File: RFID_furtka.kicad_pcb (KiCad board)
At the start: 2 copper layers, 20 parts, among them J1 CONN_01X03, Q1 SI2300DS, SW1 TSC_RELAY, U1 LDF33DT-TR, U2 MFRC522, U3 nodemcu-devkit-v1.0(ESP8266)

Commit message: Add BOM
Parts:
- moved C9 36.7 mm to (147.4, 83.5), turned to 270 degrees
- moved C7 21.9 mm to (162.8, 93.6)
- moved C8 16.8 mm to (147.4, 103.8), turned to 90 degrees
- moved J1 4.13 mm to (133.0, 80.9), turned to 0 degrees
- moved C4 2.30 mm to (132.3, 117.4)
- moved U3 0.41 mm to (154.9, 99.9), turned to 180 degrees
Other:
- board outline added: 39.3 x 59.9 mm
- net class Default: clearance 0.2 -> 0.2032; trace_width 0.25 -> 0.254
- rule trace_clearance: 0.2 -> 0.2032
- rule trace_min: 0.2 -> 0.2032
- rule via_min_drill: 0.3 -> 0.4
- rule via_min_size: 0.4 -> 0.6

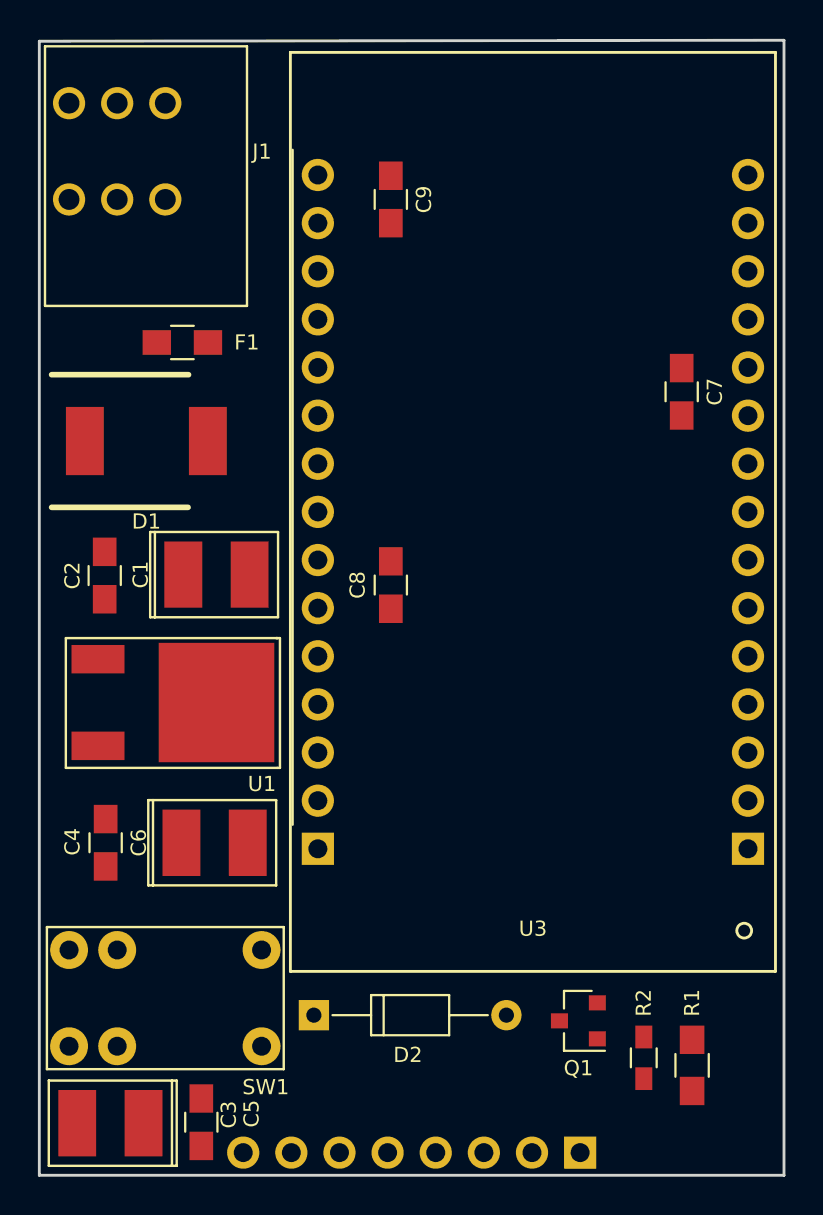
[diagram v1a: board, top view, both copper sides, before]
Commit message: Fix few 3D bugs
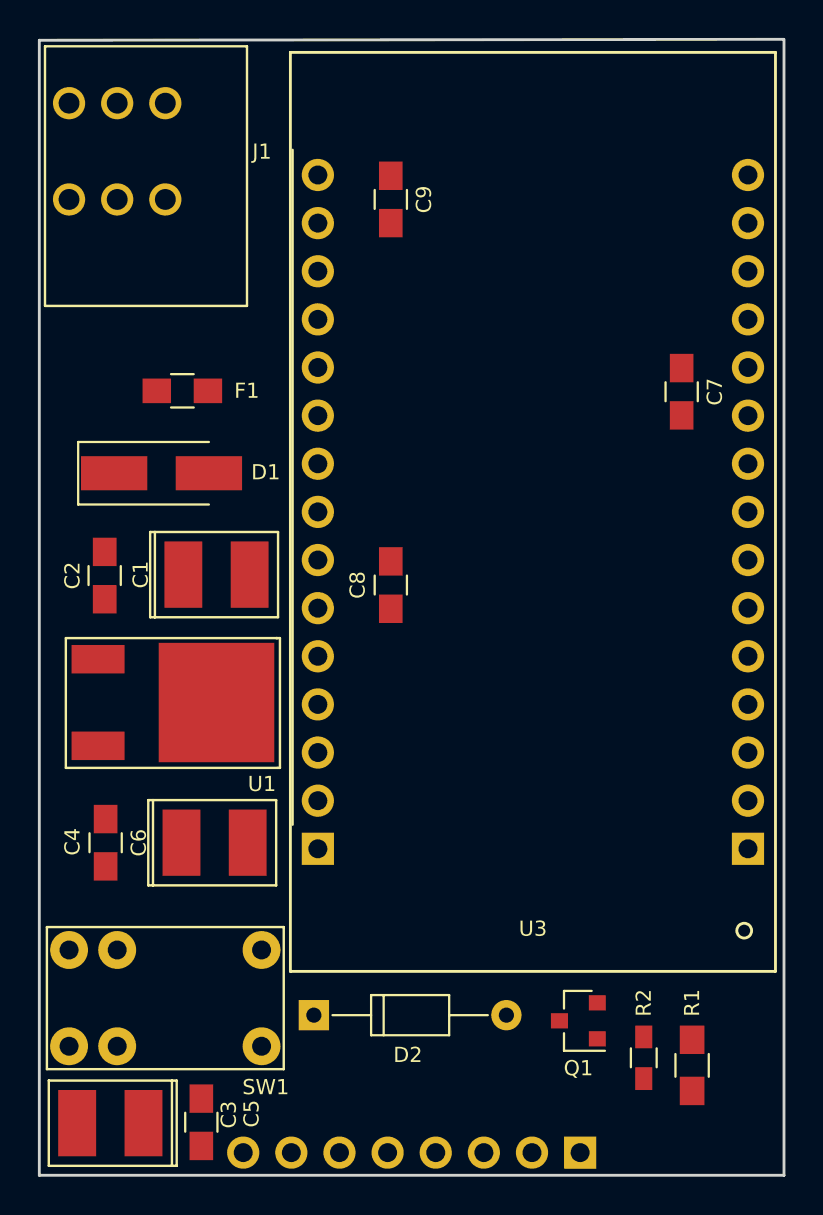
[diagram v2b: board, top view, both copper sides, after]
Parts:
- D1: footprint MyDiodesSMD:DO-214AB -> Diodes_SMD:D_SMA_Handsoldering
- moved F1 2.55 mm to (136.4, 93.5)
- moved D1 1.88 mm to (135.3, 97.9), turned to 0 degrees
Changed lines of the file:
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@@
     (links 51)
     (no_connects 51)
-    (area 127.0499 74.912899 168.341801 136.567486)
+    (area 128.774999 74.924999 168.225001 135.025001)
     (thickness 1.6)
     (drawings 4)
@@
     )
   )
-  (module MyDiodesSMD:DO-214AB (layer F.Cu)
-    (at 134.5 96.2 180)
-    (fp_text reference D1 (at 0 -4.25 180) (layer F.SilkS)
-      (effects (font (size 0.8 0.8) (thickness 0.15)))
-    )
-    (fp_text value SS34 (at -0.05 4.375 180) (layer F.Fab)
-      (effects (font (size 0.5 0.5) (thickness 0.125)))
-    )
-    (fp_line (start -5.275 3.8) (end -5.275 -3.75) (layer F.CrtYd) (width 0.1))
-    (fp_line (start 5.25 3.8) (end -5.275 3.8) (layer F.CrtYd) (width 0.1))
-    (fp_line (start 5.25 -3.775) (end 5.25 3.8) (layer F.CrtYd) (width 0.1))
-    (fp_line (start -5.25 -3.775) (end 5.25 -3.775) (layer F.CrtYd) (width 0.1))
-    (fp_line (start -2.225 3.5) (end 5 3.5) (layer F.SilkS) (width 0.3))
-    (fp_line (start -2.2 -3.5) (end 5 -3.5) (layer F.SilkS) (width 0.3))
-    (pad 1 smd rect (at 3.245 0 180) (size 2 3.6) (layers F.Cu F.Paste F.Mask)
-      (net 1 +12V))
-    (pad 2 smd rect (at -3.245 0 180) (size 2 3.6) (layers F.Cu F.Paste F.Mask)
-      (net 4 "Net-(D1-Pad2)"))
-    (model "My.3dshapes/DO-214AB(SMC).wrl"
-      (at (xyz 0 0 0))
-      (scale (xyz 0.3937 0.3937 0.3937))
-      (rotate (xyz 0 0 180))
-    )
-  )
   (module Diodes_THT:D_DO-35_SOD27_P10.16mm_Horizontal (layer F.Cu)
     (at 143.34 126.5)
@@
   )
   (module Resistors_SMD:R_0805_HandSoldering (layer F.Cu)
-    (at 136.4 91 180)
+    (at 136.4 93.55 180)
     (descr "Resistor SMD 0805, hand soldering")
     (tags "resistor 0805")
@@
       (at (xyz 0 0 0))
       (scale (xyz 1 1 1))
-      (rotate (xyz 0 0 0))
+      (rotate (xyz 0 0 90))
     )
   )
@@
     )
   )
-  (gr_line (start 168.15 75.05) (end 128.85 75.1) (layer Edge.Cuts) (width 0.15))
+  (module Diodes_SMD:D_SMA_Handsoldering (layer F.Cu)
+    (at 135.3 97.9)
+    (descr "Diode SMA (DO-214AC) Handsoldering")
+    (tags "Diode SMA (DO-214AC) Handsoldering")
+    (attr smd)
+    (fp_text reference D1 (at 5.5 -0.05) (layer F.SilkS)
+      (effects (font (size 0.8 0.8) (thickness 0.15)))
+    )
+    (fp_text value SS34 (at 0 2.6) (layer F.Fab)
+      (effects (font (size 1 1) (thickness 0.15)))
+    )
+    (fp_text user %R (at 0 -2.5) (layer F.Fab)
+      (effects (font (size 1 1) (thickness 0.15)))
+    )
+    (fp_line (start -4.4 -1.65) (end -4.4 1.65) (layer F.SilkS) (width 0.12))
+    (fp_line (start 2.3 1.5) (end -2.3 1.5) (layer F.Fab) (width 0.1))
+    (fp_line (start -2.3 1.5) (end -2.3 -1.5) (layer F.Fab) (width 0.1))
+    (fp_line (start 2.3 -1.5) (end 2.3 1.5) (layer F.Fab) (width 0.1))
+    (fp_line (start 2.3 -1.5) (end -2.3 -1.5) (layer F.Fab) (width 0.1))
+    (fp_line (start -4.5 -1.75) (end 4.5 -1.75) (layer F.CrtYd) (width 0.05))
+    (fp_line (start 4.5 -1.75) (end 4.5 1.75) (layer F.CrtYd) (width 0.05))
+    (fp_line (start 4.5 1.75) (end -4.5 1.75) (layer F.CrtYd) (width 0.05))
+    (fp_line (start -4.5 1.75) (end -4.5 -1.75) (layer F.CrtYd) (width 0.05))
+    (fp_line (start -0.64944 0.00102) (end -1.55114 0.00102) (layer F.Fab) (width 0.1))
+    (fp_line (start 0.50118 0.00102) (end 1.4994 0.00102) (layer F.Fab) (width 0.1))
+    (fp_line (start -0.64944 -0.79908) (end -0.64944 0.80112) (layer F.Fab) (width 0.1))
+    (fp_line (start 0.50118 0.75032) (end 0.50118 -0.79908) (layer F.Fab) (width 0.1))
+    (fp_line (start -0.64944 0.00102) (end 0.50118 0.75032) (layer F.Fab) (width 0.1))
+    (fp_line (start -0.64944 0.00102) (end 0.50118 -0.79908) (layer F.Fab) (width 0.1))
+    (fp_line (start -4.4 1.65) (end 2.5 1.65) (layer F.SilkS) (width 0.12))
+    (fp_line (start -4.4 -1.65) (end 2.5 -1.65) (layer F.SilkS) (width 0.12))
+    (pad 1 smd rect (at -2.5 0) (size 3.5 1.8) (layers F.Cu F.Paste F.Mask)
+      (net 1 +12V))
+    (pad 2 smd rect (at 2.5 0) (size 3.5 1.8) (layers F.Cu F.Paste F.Mask)
+      (net 4 "Net-(D1-Pad2)"))
+    (model Diodes_SMD.3dshapes/D_SMA_Handsoldering.wrl
+      (at (xyz 0 0 0))
+      (scale (xyz 0.3937 0.3937 0.3937))
+      (rotate (xyz 0 0 0))
+    )
+  )
+  (gr_line (start 168.15 75) (end 128.85 75.05) (layer Edge.Cuts) (width 0.15))
   (gr_line (start 168.15 134.95) (end 168.15 75.05) (layer Edge.Cuts) (width 0.15))
   (gr_line (start 128.85 134.95) (end 168.15 134.95) (layer Edge.Cuts) (width 0.15))
-  (gr_line (start 128.85 75.1) (end 128.85 134.95) (layer Edge.Cuts) (width 0.15))
+  (gr_line (start 128.85 75.05) (end 128.85 134.95) (layer Edge.Cuts) (width 0.15))
 )

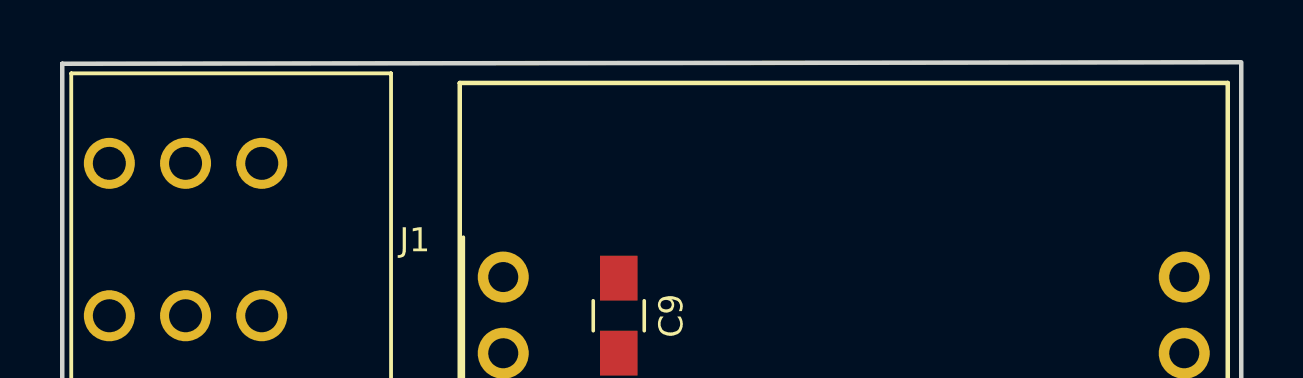
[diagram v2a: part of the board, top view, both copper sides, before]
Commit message: Fix edge cuts
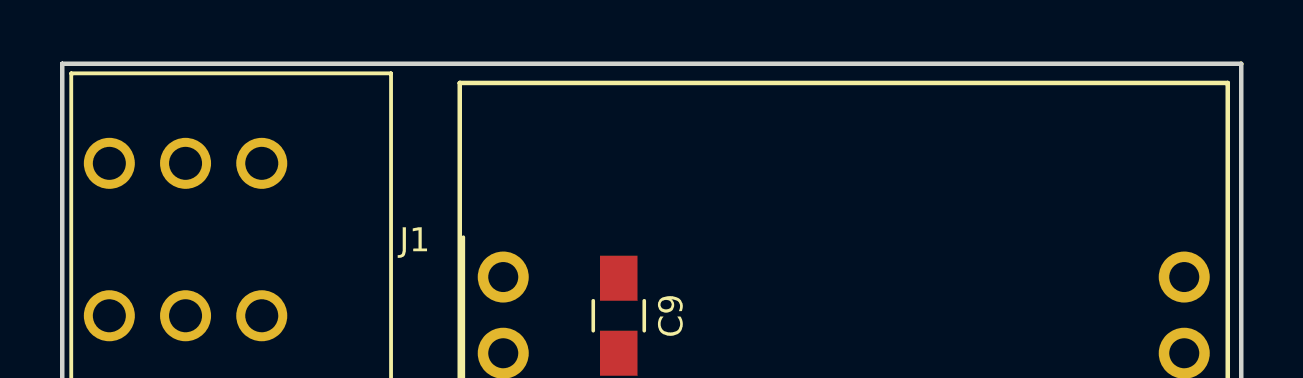
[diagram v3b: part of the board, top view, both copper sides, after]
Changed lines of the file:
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@@
     )
   )
-  (gr_line (start 168.15 75) (end 128.85 75.05) (layer Edge.Cuts) (width 0.15))
+  (gr_line (start 168.15 75.05) (end 128.85 75.05) (layer Edge.Cuts) (width 0.15))
   (gr_line (start 168.15 134.95) (end 168.15 75.05) (layer Edge.Cuts) (width 0.15))
   (gr_line (start 128.85 134.95) (end 168.15 134.95) (layer Edge.Cuts) (width 0.15))

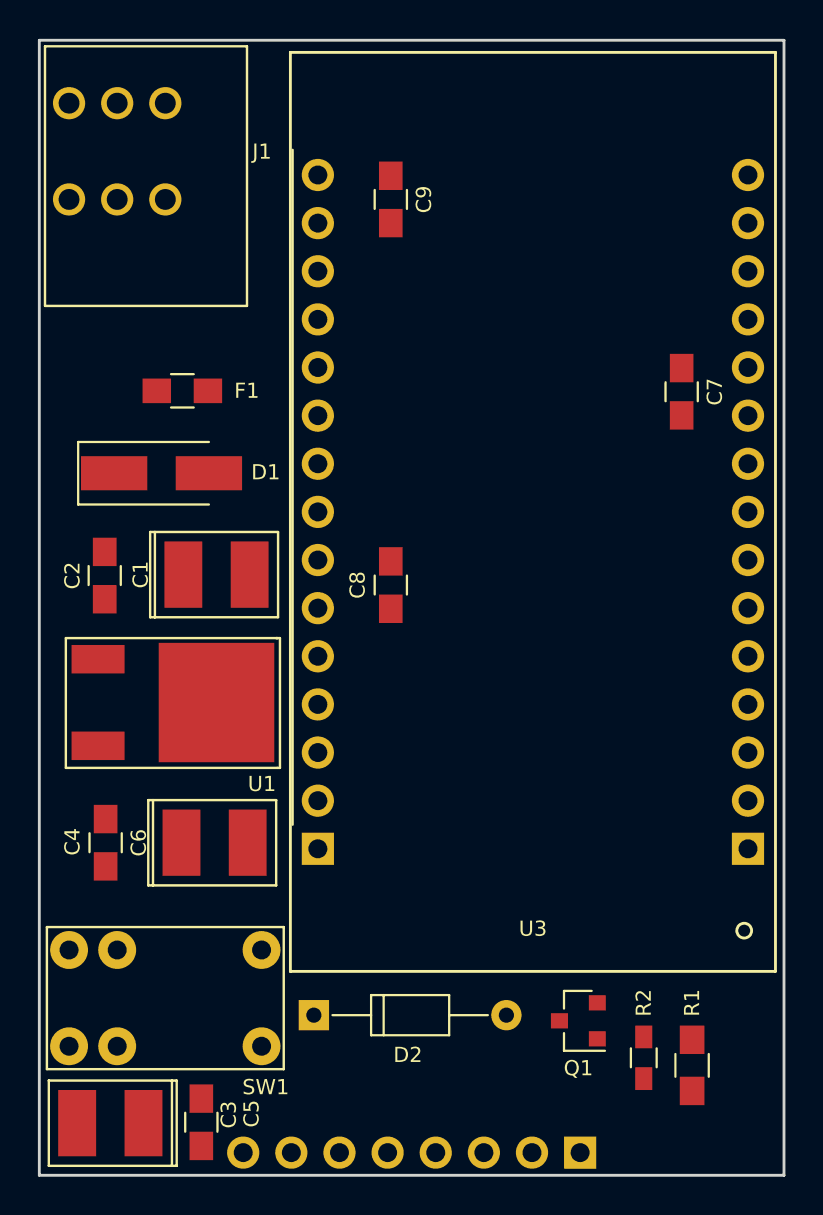
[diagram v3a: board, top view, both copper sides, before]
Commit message: All signals routed without GND
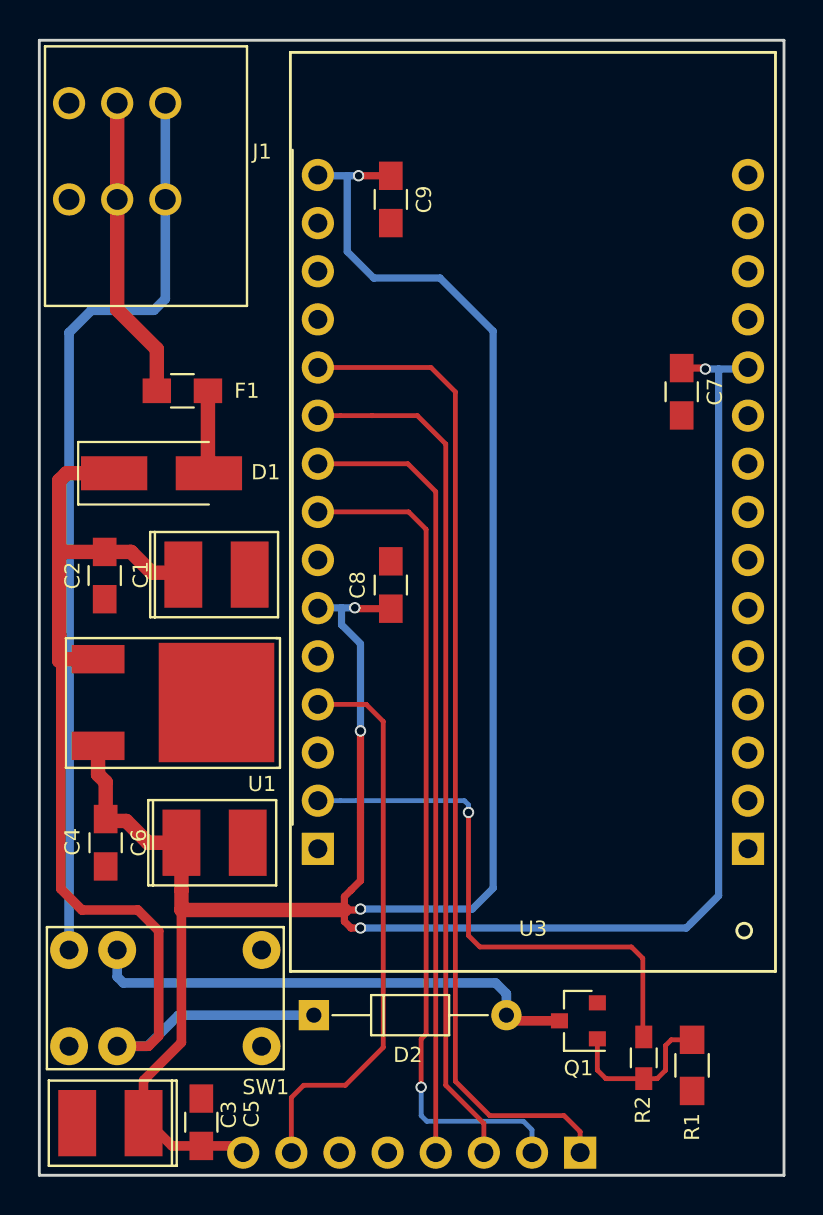
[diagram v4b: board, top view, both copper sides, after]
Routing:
- net +3V3: track 0.00 -> 168.9 mm, vias 0 -> 6
- net +12V: track 0.00 -> 59.7 mm
- net /SDA: track 0.00 -> 53.0 mm
- net /relay: track 0.00 -> 48.7 mm
- net /MOSI: track 0.00 -> 45.6 mm
- net /SCK: track 0.00 -> 44.5 mm, vias 0 -> 1
- net /MISO: track 0.00 -> 41.7 mm
- net /RST: track 0.00 -> 29.9 mm
- net /open/close: track 0.00 -> 28.8 mm, vias 0 -> 1
- net Net-(D2-Pad2): track 0.00 -> 26.4 mm
- net Net-(F1-Pad2): track 0.00 -> 16.0 mm
- net Net-(Q1-Pad1): track 0.00 -> 8.45 mm
- net Net-(D1-Pad2): track 0.00 -> 4.37 mm
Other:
- net class Default: clearance 0.2032 -> 0.254
- rule trace_clearance: 0.2032 -> 0.254

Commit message: Add GND vias
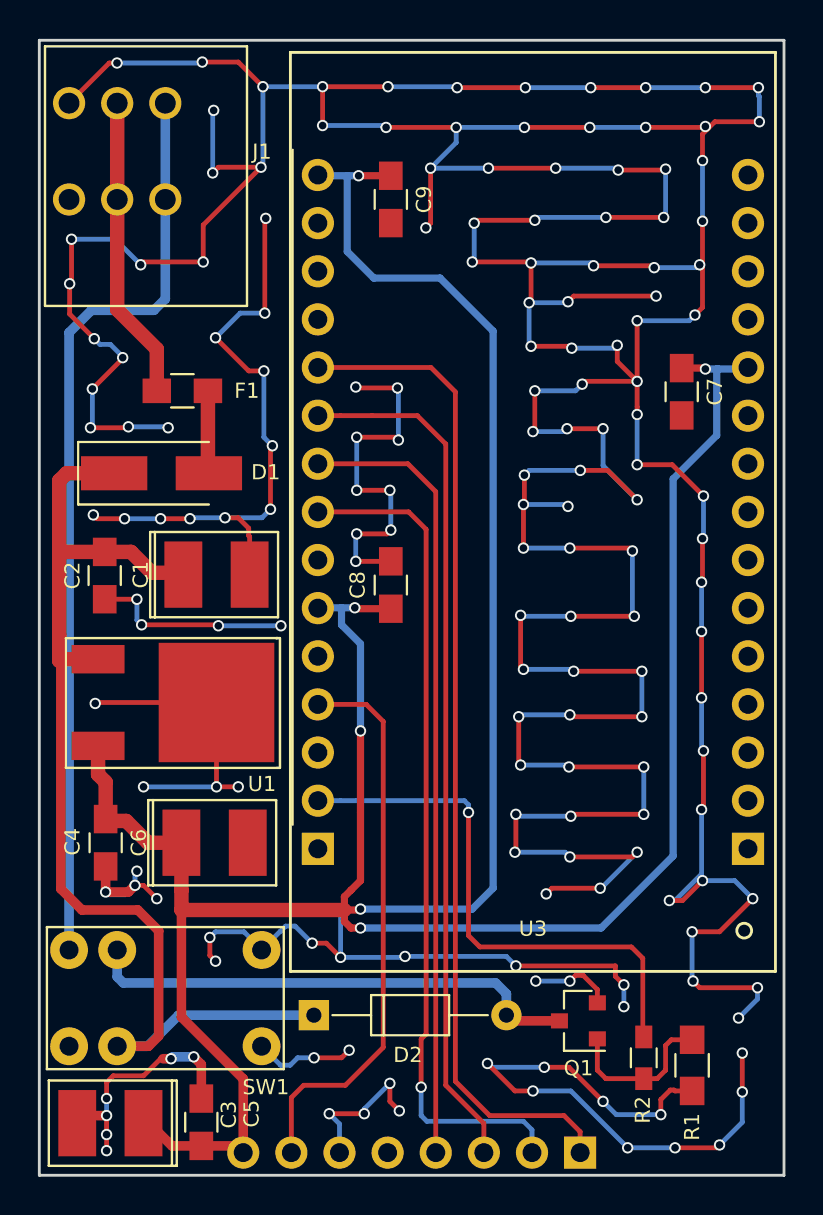
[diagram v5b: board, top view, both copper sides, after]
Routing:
- net GND: track 0.00 -> 507.8 mm, vias 0 -> 171
- net +3V3: track 168.9 -> 166.3 mm
- added copper zone on B.Cu, net GND
- added copper zone on F.Cu, net GND

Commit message: Add some comments and production files
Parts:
- moved R1 8.04 mm to (155.3, 129.9), turned to 180 degrees
- moved R2 3.83 mm to (162.7, 125.5), turned to 180 degrees
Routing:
- net GND: track 507.8 -> 466.5 mm, vias 171 -> 161
- net Net-(Q1-Pad1): track 8.45 -> 10.9 mm
- net /open/close: track 28.8 -> 27.4 mm
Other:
- board text added: "12V"
- board text added: "GND"
- board text added: "OUT"
